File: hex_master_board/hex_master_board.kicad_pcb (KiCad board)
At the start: 2 copper layers, 114 parts, among them J1 USB_B_Micro, SW1 SW_DIP_x01, SW10 SW_DIP_x01, SW11 SW_DIP_x01, SW12 SW_DIP_x01, SW2 SW_DIP_x01, SW3 SW_DIP_x01, SW4 SW_DIP_x01, SW5 SW_DIP_x01, SW6 SW_DIP_x01, SW7 SW_DIP_x01, SW8 SW_DIP_x01, SW9 SW_DIP_x01, U1 Jack_CP-002B-ND, U10 EXB-2HV221JV, U11 EXB-2HV221JV, U12 Jack_CP-002B-ND, U13 Servo_connector, U14 Servo_connector, U15 Servo_connector, U16 Servo_connector, U17 Servo_connector, U18 Servo_connector, U19 Servo_connector, U2 74LVC1G157GV_MUX2, U20 Servo_connector, U21 Servo_connector, U22 Servo_connector, U23 Servo_connector, U24 Servo_connector, U25 Servo_connector, U26 Servo_connector, U27 Servo_connector, U28 Servo_connector, U29 EXB-2HV221JV, U3 AP2210N-5.0TRG1-lin-reg, U30 EXB-2HV221JV, U31 Servo_connector, U32 Servo_connector, U33 Servo_connector, U34 Servo_connector, U35 Servo_connector, U36 Servo_connector, U37 Servo_connector, U38 Servo_connector, U39 Servo_connector, U4 FT232RL, U40 Servo_connector, U41 Servo_connector, U42 Servo_connector, U43 Servo_connector, U44 Servo_connector, U45 Servo_connector, U46 Servo_connector, U47 ICSP_breakout, U48 header_0.1_8_powered, U49 header_0.1_8, U5 TPS2113A, U50 header_0.1_8, U51 LIS3DH_breakout, U52 header_0.1_I2C, U6 Pushbutton_Stockroom, U7 ATmega2561-16AU, U8 PCA9685PW, U9 PCA9685PW, Y1 Crystal

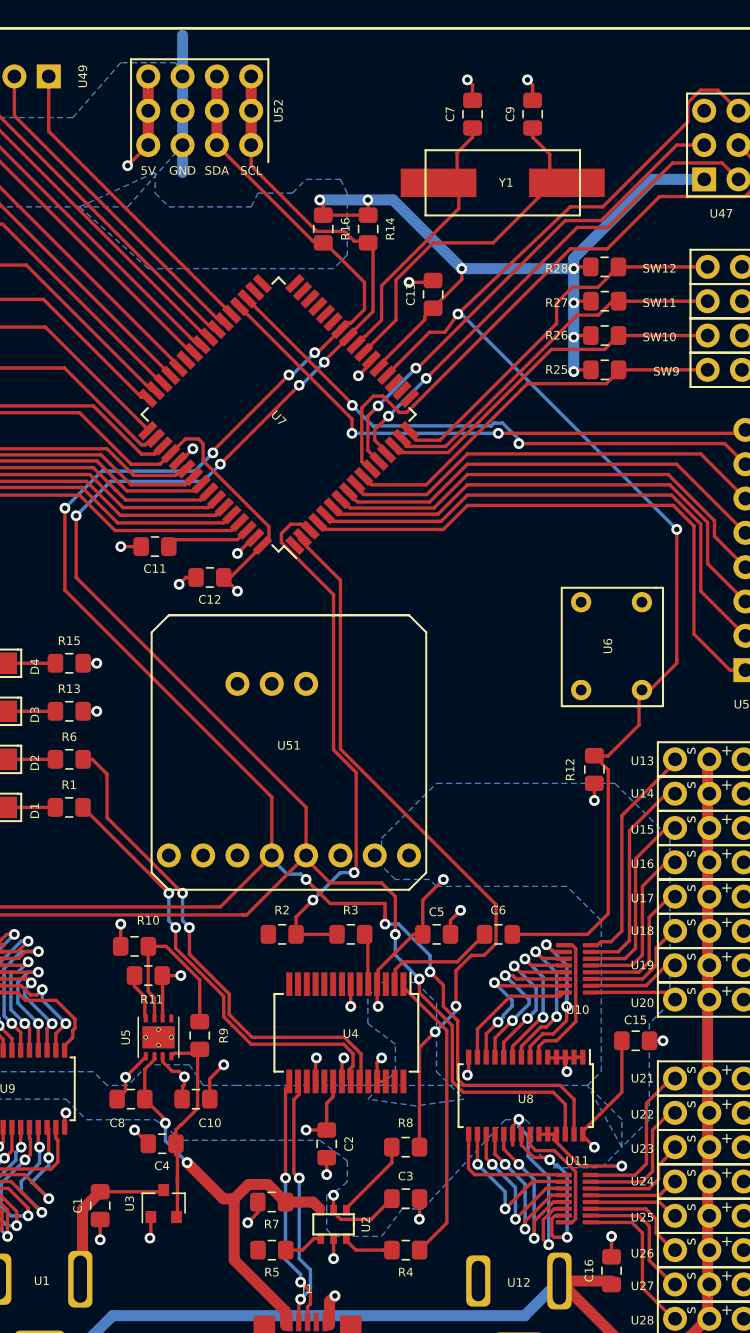
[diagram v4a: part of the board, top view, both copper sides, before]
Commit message: Integrate XBEE... Functionality on first-pass PCB is done!
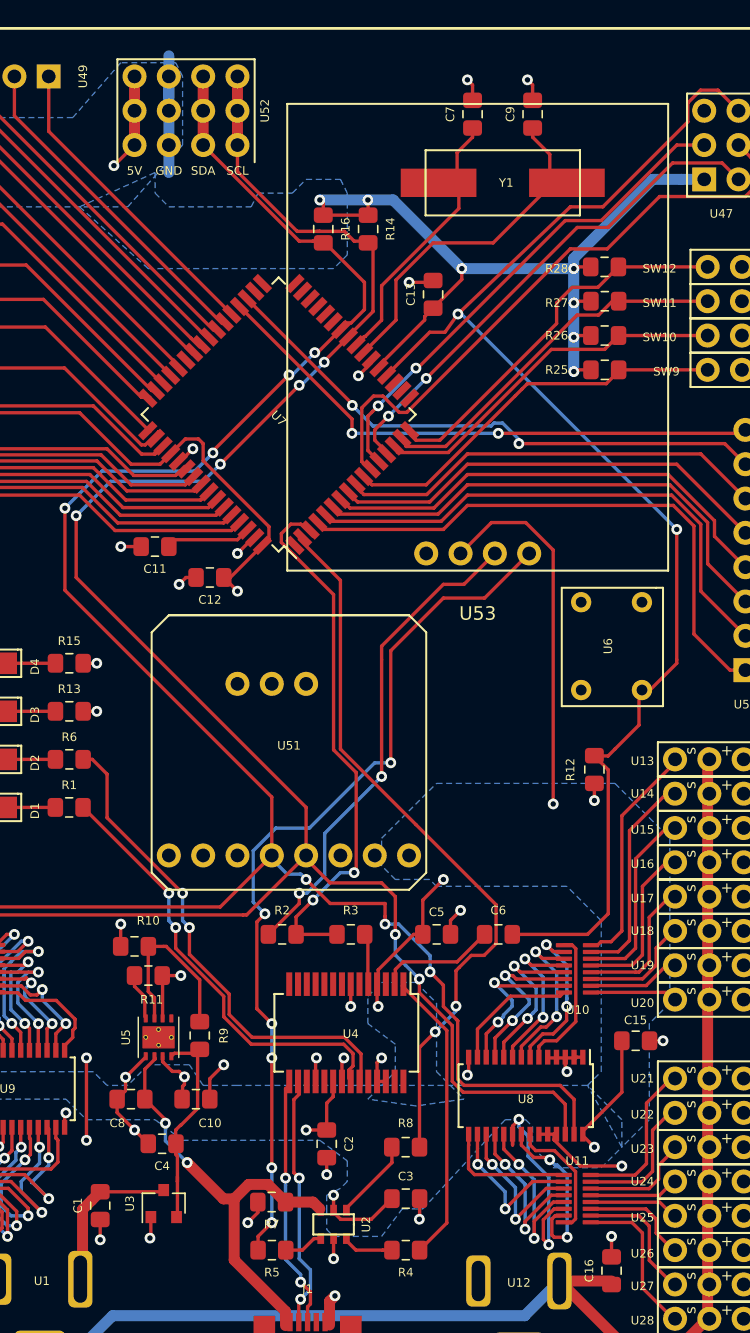
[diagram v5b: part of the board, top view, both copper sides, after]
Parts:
- added U53: header_0.1_xbee, hex_master_board:header_0.1_xbee, F.Cu at (52.8, 40.1)
- moved U52 1.02 mm to (31.2, 2.29)
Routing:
- net /XBEE_TXD: track 0.00 -> 65.1 mm, vias 0 -> 6
- net /XBEE_RXD: track 0.00 -> 36.0 mm, vias 0 -> 2
- net +5V: track 210.9 -> 238.7 mm, vias 31 -> 32
- net GND: track 83.1 -> 92.0 mm, vias 36 -> 38
- net /SCL: track 154.1 -> 155.6 mm
- net /SDA: track 153.9 -> 154.9 mm

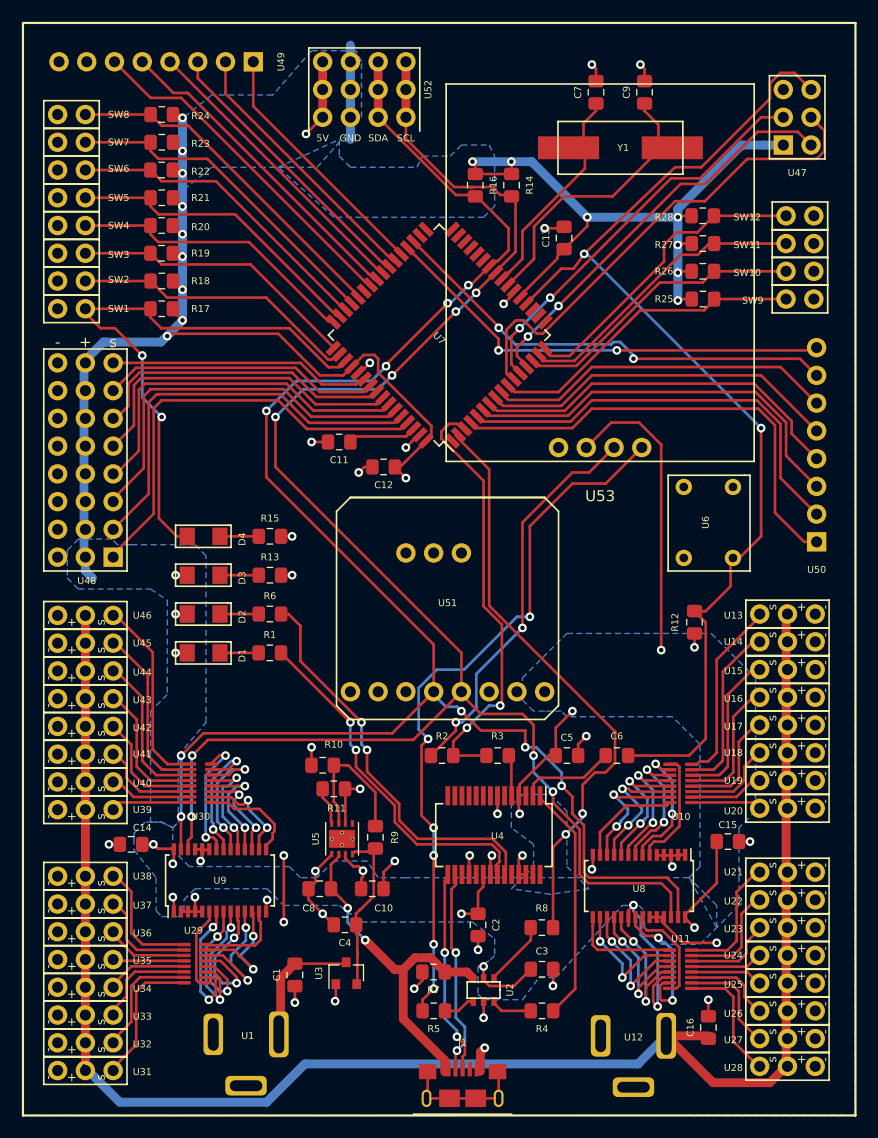
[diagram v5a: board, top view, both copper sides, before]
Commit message: Add silk screen labels and olin logo
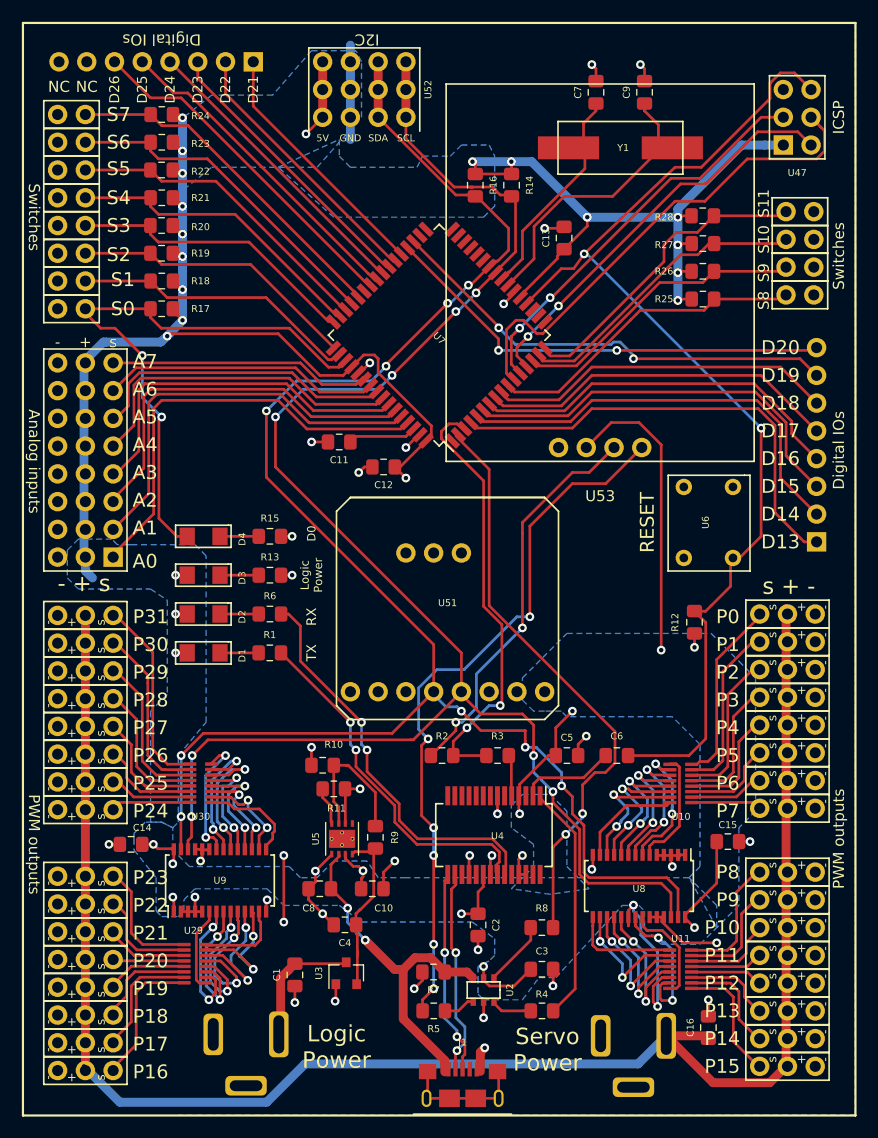
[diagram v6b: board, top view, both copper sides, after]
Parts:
- removed SW10, SW11, SW12, SW9: SW_DIP_x01, hex_master_board:switch_ins
- added ?: , , F.Cu at (7.11, 3.56)
- added ?: , , F.Cu at (3.81, 2.54)
- added ?: , , F.Cu at (2.29, 3.30)
- added ?: , , F.Cu at (0.00, 0.00)
- added ?: , , F.Cu at (16.5, 2.03)
- added ?: , , F.Cu at (14.0, 2.03)
- added ?: , , F.Cu at (14.0, 5.84)
- added ?: , , F.Cu at (3.30, 28.4)
- added G***: LOGO, hex_master_board:olin_logo, B.Cu at (39.6, 49.3)
- added S10: SW_DIP_x01, hex_master_board:switch_ins, F.Cu at (67.3, 19.8)
- added S11: SW_DIP_x01, hex_master_board:switch_ins, F.Cu at (67.3, 17.3)
- added S8: SW_DIP_x01, hex_master_board:switch_ins, F.Cu at (67.3, 24.9)
- added S9: SW_DIP_x01, hex_master_board:switch_ins, F.Cu at (67.3, 22.4)
- renumbered SW1 to S0, SW2 to S1, SW3 to S2, SW4 to S3, SW5 to S4, SW6 to S5, SW7 to S6, SW8 to S7
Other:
- board text added: "- + s"
- board text added: "A0"
- board text added: "A1"
- board text added: "A2"
- board text added: "A3"
- board text added: "A4"
- board text added: "A5"
- board text added: "A6"
- board text added: "A7"
- board text added: "Analog inputs"
- board text added: "D0"
- board text added: "D13"
- board text added: "D14"
- board text added: "D15"
- board text added: "D16"
- board text added: "D17"
- board text added: "D18"
- board text added: "D19"
- board text added: "D20"
- board text added: "Digital IOs"
- board text added: "I2C"
- board text added: "ICSP"
- board text added: "Logic Power"
- board text added: "P0"
- board text added: "P1"
- board text added: "P10"
- board text added: "P11"
- board text added: "P12"
- board text added: "P13"
- board text added: "P14"
- board text added: "P15"
- board text added: "P16"
- board text added: "P17"
- board text added: "P18"
- board text added: "P19"
- board text added: "P2"
- board text added: "P20"
- board text added: "P21"
- board text added: "P22"
- board text added: "P23"
- board text added: "P24"
- board text added: "P25"
- board text added: "P26"
- board text added: "P27"
- board text added: "P28"
- board text added: "P29"
- board text added: "P3"
- board text added: "P30"
- board text added: "P31"
- board text added: "P4"
- board text added: "P5"
- board text added: "P6"
- board text added: "P7"
- board text added: "P8"
- board text added: "P9"
- board text added: "PWM outputs"
- board text added: "RESET"
- board text added: "RX"
- board text added: "Servo Power"
- board text added: "Switches"
- board text added: "TX"
- board text added: "s + -"
